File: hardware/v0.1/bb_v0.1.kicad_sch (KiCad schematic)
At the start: 11 parts, among them U1 MCP1640Cx-xCHY, U2 MAX16054AZT_T

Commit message: first commit of full schematic
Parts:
- added C10, C13, C14, C6, C8: 100n, symbol Device:C
- added C11, C12, C3, C4: 22p, symbol Device:C
- added C5: 1u, symbol Device:C
- added C7, C9: 10u, symbol Device:C
- added D1, D2: LESD5D5.0CT1G, LESD5D5.0CT1G:TVS_LESD5D5.0CT1G, symbol LESD5D5.0CT1G:LESD5D5.0CT1G
- added D3, D4, D5: LED, symbol Device:LED
- added J1: USB_B_Micro, symbol Connector:USB_B_Micro
- added J2: Conn_01x02, symbol Connector_Generic:Conn_01x02
- added J3: Conn_01x05, symbol Connector_Generic:Conn_01x05
- added L2: 3u3, symbol Device:L
- added Q1: MMBT4403_, MMBT4403_:SOT23-BEC, symbol MMBT4403_:MMBT4403_
- added R10, R13, R3, R9: 10k, symbol Device:R
- added R11: 8k2, symbol Device:R
- added R12: 20k, symbol Device:R
- added R14, R15: 100, symbol Device:R
- added R4, R5: 0, symbol Device:R
- added R6, R7, R8: 4k7, symbol Device:R
- added U3: ESP32-C3-WROOM-02, RF_Module:ESP32-C3-WROOM-02, symbol RF_Module:ESP32-C3-WROOM-02
- added U4: HX711, Package_SO:SOP-16_3.9x9.9mm_P1.27mm, symbol Analog_ADC:HX711
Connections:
- net 3V3: now also C2.2, C14.2, C6.2, C7.2, C8.1, C9.1, J2.2 (Pin_2), Q1.E, R10.1, R3.1, R7.1, R9.1, U3.1 (3V3), U4.1 (VSUP), U4.16 (DVDD); no longer C2.1
- net 3V3EN: now also R6.1
- net GND: now also C2.1, C10.1, C11.1, C12.1, C14.1, C3.2, C4.2, C5.1, C6.1, C7.1, C8.2, C9.2, D1.2, D2.2, J1.5 (GND), J1.6 (Shield), J3.1 (Pin_1), J3.4 (Pin_4), R11.2, R13.2, R4.2, R5.2, U3.19 (GND), U3.9 (GND), U4.14 (XI), U4.5 (AGND); no longer C2.2
- new net: D4.2 (A), R7.2
- new net: D3.2 (A), R6.2
- new net: L2.2, Q1.C, R12.1, U4.3 (AVDD)
- new net: R11.1, R12.2
- new net: R5.1, U3.11 (IO20/RXD)
- new net: C5.2, R3.2, U3.2 (EN)
- new net: Q1.B, U4.2 (BASE)
- new net: R4.1, U3.12 (IO21/TXD)
- new net: J2.1 (Pin_1), R13.1, U4.15 (RATE)
- new net: C10.2, U4.6 (VBG)
- new net: D5.2 (A), R8.2
- new net A+: J3.3 (Pin_3), R14.1
- new net A-: J3.2 (Pin_2), R15.1
- new net AVDD: C11.2, C12.2, J3.5 (Pin_5), L2.1
- new net D+: C3.1, D1.1, J1.3 (D+), U3.14 (IO19)
- new net D-: C4.1, D2.1, J1.2 (D-), U3.13 (IO18)
- new net GPIO4: R8.1, U3.3 (IO4)
- new net GPIO8: R9.2, U3.7 (IO8)
- new net GPIO9: R10.2, U3.8 (IO9)
- new net HXA+: C13.2, R14.2, U4.8 (INA+)
- new net HXA-: C13.1, R15.2, U4.7 (INA-)
- new net HXSCLK: U3.4 (IO5), U4.11 (PD_SCK)
- new net HXSDATA: U3.5 (IO6), U4.12 (DOUT)
- no-connect marks 0 -> 5
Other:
- note added: "ESP32"
- note added: "HX711"
- note added: "LED and misc"
- note added: "USB Connector"
- moved on the sheet: C2

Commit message: fixed schematic
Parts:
- removed L1: 4u7, symbol Device:L
- added L1: WE-TPC_2813, WE-TPC_2813:WE-TPC_2813, symbol WE-TPC_2813:WE-TPC_2813
- C1, C10, C11, C12, C13, C14, C2, C3, C4, C5, C6, C7, C8, C9: footprint (none) -> Capacitor_SMD:C_0603_1608Metric_Pad1.08x0.95mm_HandSolder
- D3, D4, D5: footprint (none) -> LED_SMD:LED_0603_1608Metric_Pad1.05x0.95mm_HandSolder
- J1, J2, J3: footprint (none) -> TestPoint:TestPoint_Pad_1.0x1.0mm
- L2: footprint (none) -> Inductor_SMD:L_0603_1608Metric_Pad1.05x0.95mm_HandSolder
- R1, R10, R11, R12, R13, R14, R15, R2, R3, R4, R5, R6, R7, R8, R9: footprint (none) -> Resistor_SMD:R_0603_1608Metric_Pad0.98x0.95mm_HandSolder
- TP1, TP2, TP3, TP4: footprint (none) -> TestPoint:TestPoint_Pad_D2.5mm
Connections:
- net 3V3EN: no longer R6.1
- net A3V3EN: now also R6.1
- net BATT3V: now also L1.1
- net GND: now also D3.1 (K), D4.1 (K), D5.1 (K)
- net at R11.1, R12.2: now also U4.4 (VFB)
- net at U1.1 (SW): now also L1.2
- no-connect marks 5 -> 11

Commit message: first complete layout
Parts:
- removed J2: Conn_01x02, TestPoint:TestPoint_Pad_1.0x1.0mm, symbol Connector_Generic:Conn_01x02
- removed J3: Conn_01x05, TestPoint:TestPoint_Pad_1.0x1.0mm, symbol Connector_Generic:Conn_01x05
- added H1, H2, H3, H4, H5, H6: MountingHole, MountingHole:MountingHole_2.2mm_M2, symbol Mechanical:MountingHole
- added JP1: Jumper_2_Bridged, Jumper:SolderJumper-2_P1.3mm_Open_RoundedPad1.0x1.5mm, symbol Jumper:Jumper_2_Bridged
- added SW1: SW_Omron_B3FS, Button_Switch_SMD:SW_SPST_Omron_B3FS-101xP, symbol Switch:SW_Omron_B3FS
- added TP5: TestPoint, TestPoint:TestPoint_Pad_2.0x2.0mm, symbol Connector:TestPoint
- added TP6: SHIELD, TestPoint:TestPoint_Pad_2.0x2.0mm, symbol Connector:TestPoint
- added TP7: BATTGND, TestPoint:TestPoint_Pad_2.0x2.0mm, symbol Connector:TestPoint
- D1, D2: footprint LESD5D5.0CT1G:TVS_LESD5D5.0CT1G -> mod:TVS_LESD5D5.0CT1G
- J1: footprint TestPoint:TestPoint_Pad_1.0x1.0mm -> Connector_USB:USB_Micro-B_Amphenol_10118194-0001LF_Horizontal
- L1: footprint WE-TPC_2813:WE-TPC_2813 -> mod:WE-TPC_2813
- Q1: footprint MMBT4403_:SOT23-BEC -> mod:SOT23-BEC
- TP1: value Batt IN -> BATTIN_TP; footprint TestPoint:TestPoint_Pad_D2.5mm -> TestPoint:TestPoint_Pad_2.0x2.0mm
- TP2: value Batt GND -> TestPoint; footprint TestPoint:TestPoint_Pad_D2.5mm -> TestPoint:TestPoint_Pad_2.0x2.0mm
- TP3: value Sw IN -> TestPoint; footprint TestPoint:TestPoint_Pad_D2.5mm -> TestPoint:TestPoint_Pad_2.0x2.0mm
- TP4: value Sw OUT -> TestPoint; footprint TestPoint:TestPoint_Pad_D2.5mm -> TestPoint:TestPoint_Pad_2.0x2.0mm
- U2: footprint MAX16054AZT_T:SOT95P275X110-6N -> mod:SOT95P275X110-6N
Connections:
- net 3V3: now also JP1.2 (B)
- net A+: now also TP3.1
- net A-: now also TP4.1
- net A3V3EN: now also D3.1 (K); no longer R6.1
- net AVDD: now also TP2.1
- net BATT3V: now also R6.1, SW1.1; no longer TP3.1
- net GND: now also TP5.1, TP6.1, TP7.1; no longer D3.1 (K), TP2.1
- net SWOUT: now also SW1.2; no longer TP4.1
- net at R13.1, U4.15 (RATE): now also JP1.1 (A)
- net GPIO3: now reaches U3.15 (IO3)
- no-connect marks 11 -> 10
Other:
- note added: "Connectors and switches"
- note added: "Power Latch"
- note removed: "Power ON/OFF"
- moved on the sheet: C13, C5, C6, C7, R14, R15, R3, R4, R5, TP1, U2, U3

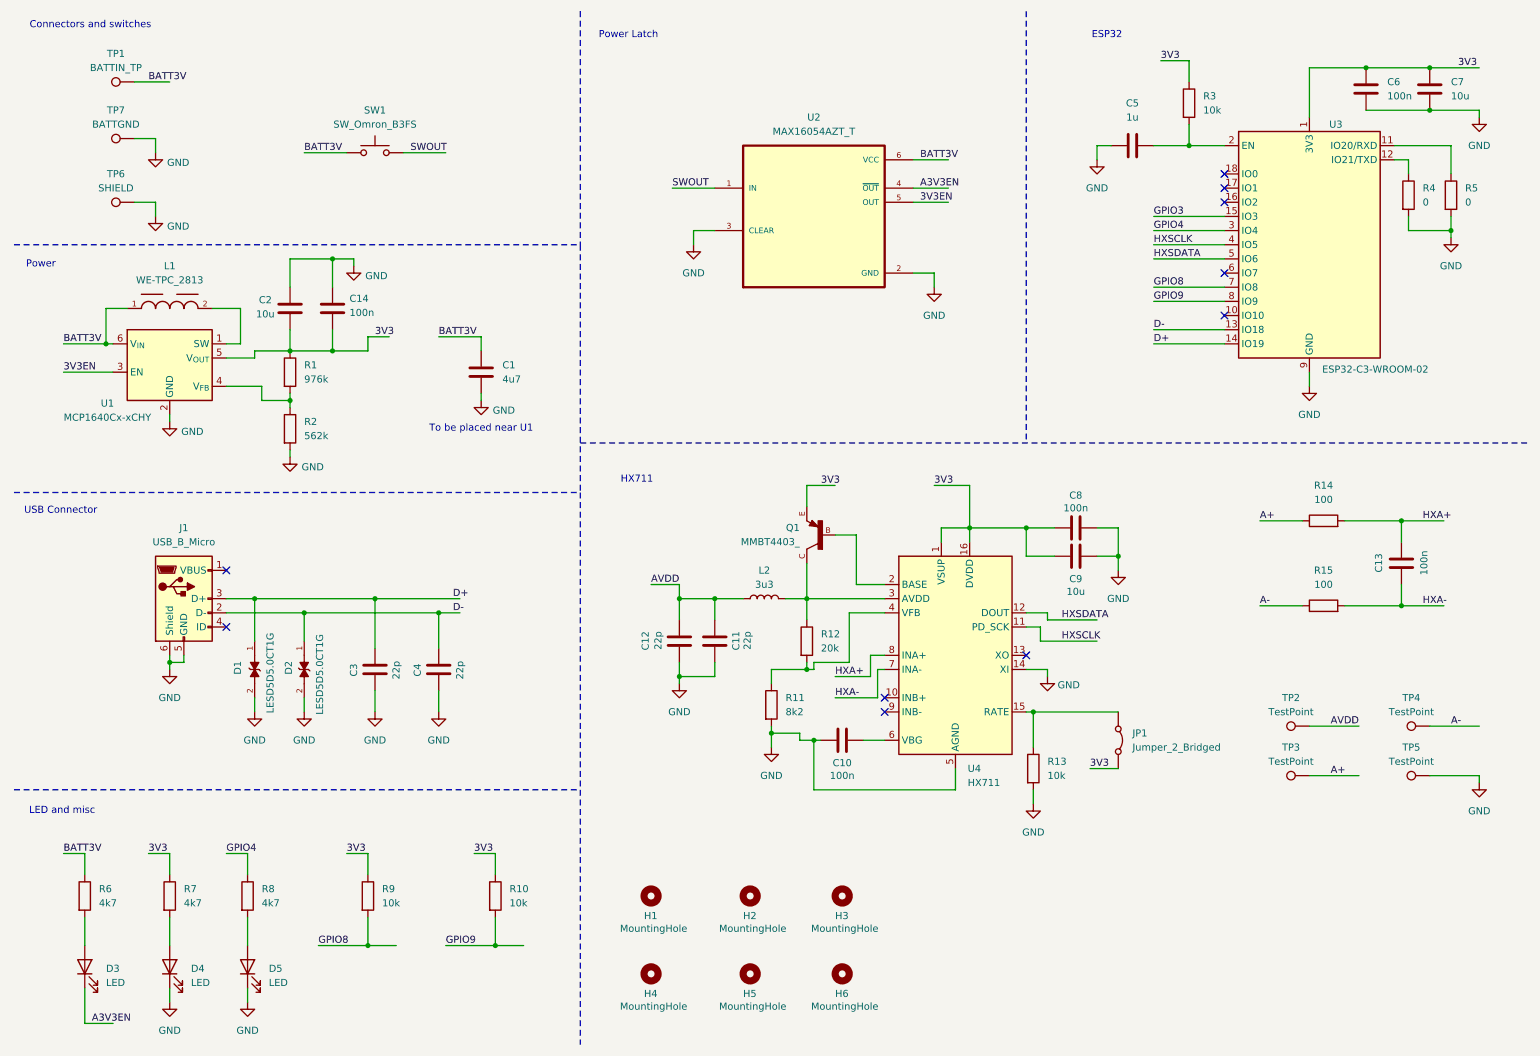
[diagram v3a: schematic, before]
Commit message: added button
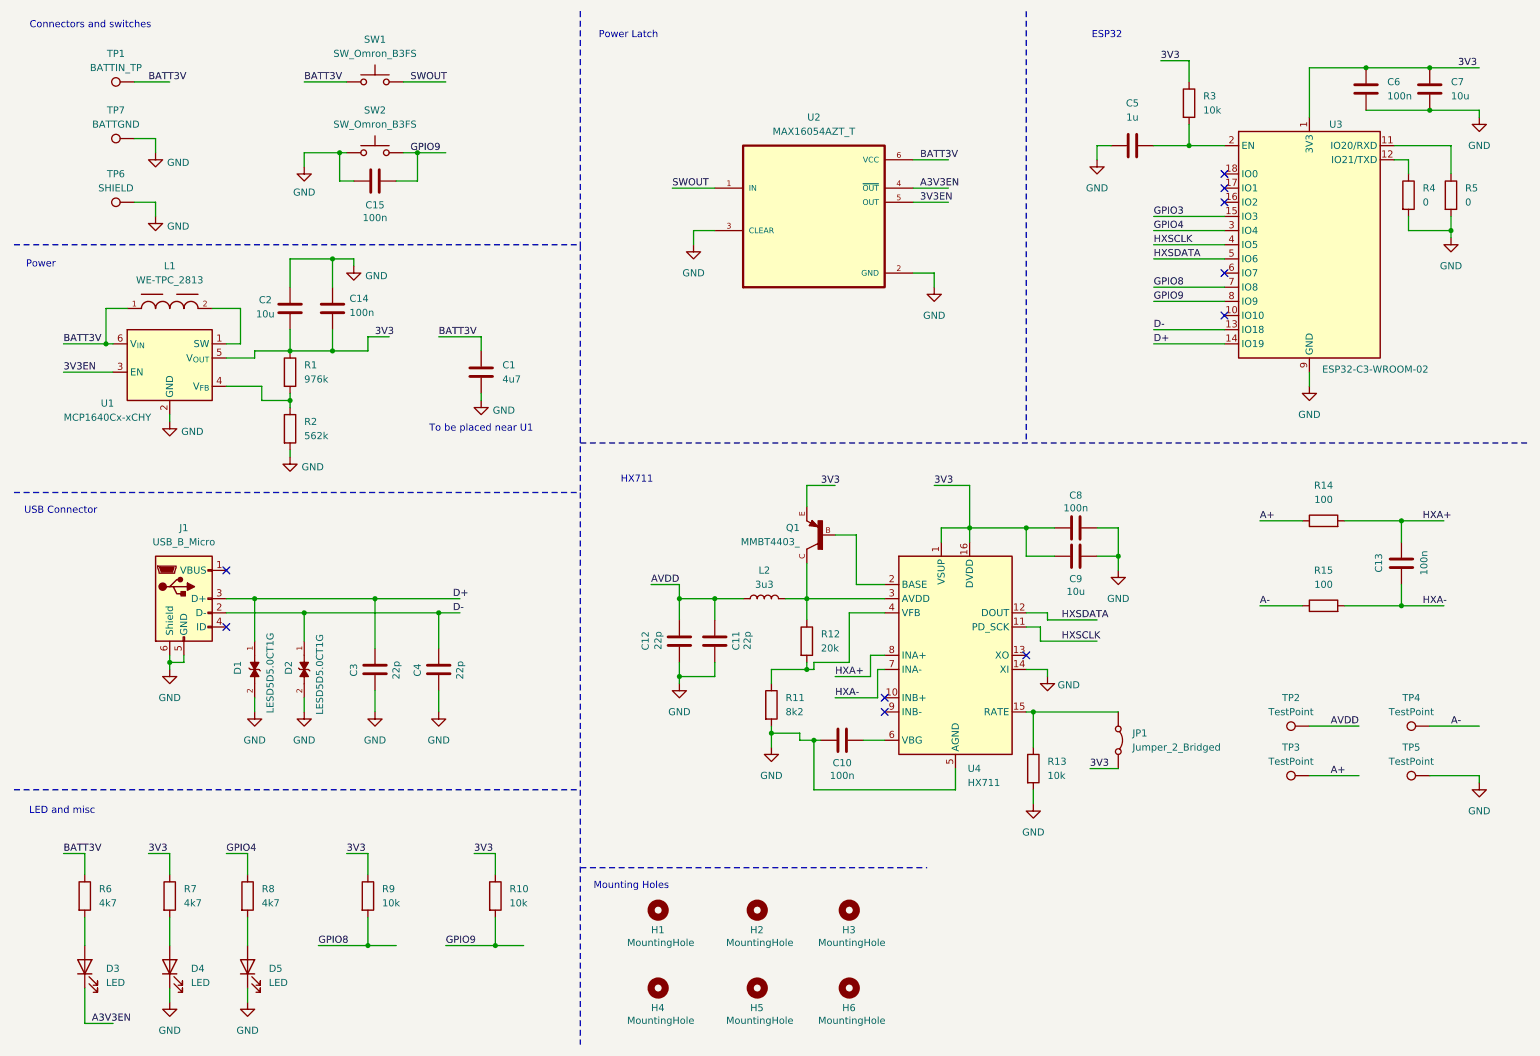
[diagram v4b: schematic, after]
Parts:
- added C15: 100n, Capacitor_SMD:C_0603_1608Metric_Pad1.08x0.95mm_HandSolder, symbol Device:C
- added SW2: SW_Omron_B3FS, Button_Switch_SMD:SW_SPST_Omron_B3FS-101xP, symbol Switch:SW_Omron_B3FS
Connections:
- net GND: now also C15.1, SW2.1
- net GPIO9: now also C15.2, SW2.2
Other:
- note added: "Mounting Holes"
- moved on the sheet: H1, H2, H3, H4, H5, H6, SW1

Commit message: fixed oversights after first iteration
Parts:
- removed R4, R5: 0, Resistor_SMD:R_0603_1608Metric_Pad0.98x0.95mm_HandSolder, symbol Device:R
- removed U1: MCP1640Cx-xCHY, Package_TO_SOT_SMD:SOT-23-6, symbol Regulator_Switching:MCP1640Cx-xCHY
- added U1: MCP1640Bx-xCHY, Package_TO_SOT_SMD:SOT-23-6, symbol Regulator_Switching:MCP1640Bx-xCHY
- C11: value 22p -> 10u
- C12: value 22p -> 100n
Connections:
- net 3V3: now also U1.5 (V_{OUT})
- net 3V3EN: now also U1.3 (EN)
- net BATT3V: now also U1.6 (V_{IN}); no longer SW1.1
- net GND: now also SW1.1, U1.2 (GND)
- net at R1.2, R2.1: now also U1.4 (V_{FB})
- net at L1.2: now also U1.1 (SW)
- no-connect marks 10 -> 12
